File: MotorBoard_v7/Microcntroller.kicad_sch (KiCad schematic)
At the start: 30 parts, among them J1 5Vsel, J10 XDS_VCC, J2 1725656, J2_J4 LaunchPad, J3_J1 LaunchPad, J5 KK-396, J6 11.1V, U1 LM2596S-5.0_NOPB, U2 LM2937ESX-3.3_NOPB, U3 SSD1306

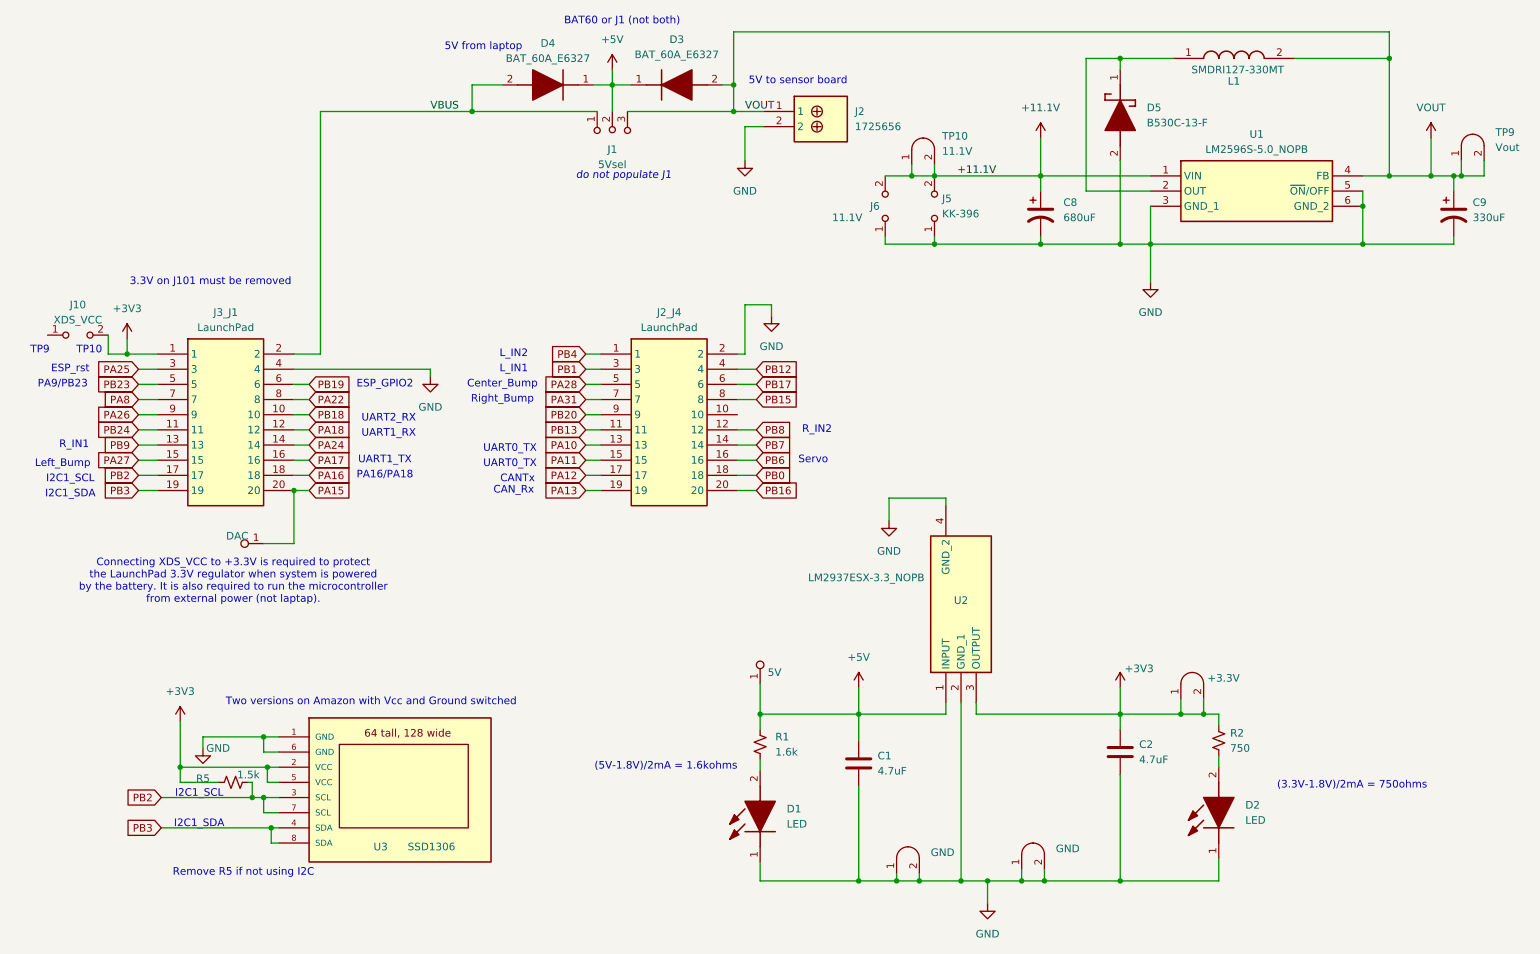
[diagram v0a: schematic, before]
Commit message: added lab 6 update starter files
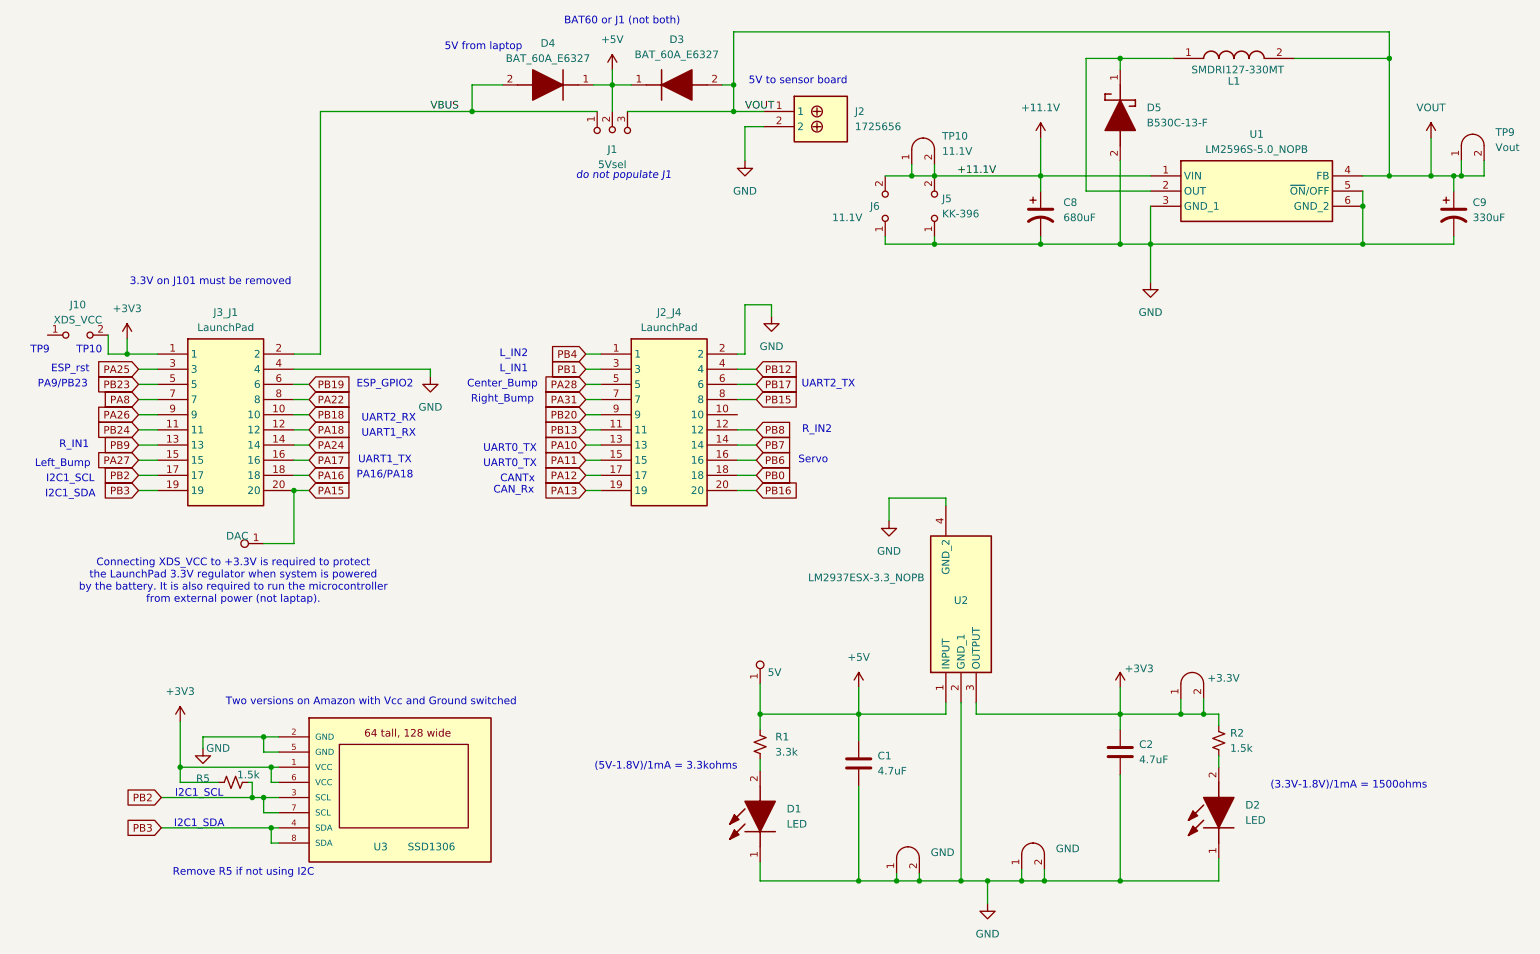
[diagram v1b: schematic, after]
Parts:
- R1: value 1.6k -> 3.3k
- R2: value 750 -> 1.5k
- U3: footprint RSLK2:SSD1306 -> ECE445L:SSD1306; symbol RSLK2:SSD1306 -> ECE445L:SSD1306
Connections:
- net +3V3: now also U3.1 (VCC), U3.6 (VCC); no longer U3.2 (VCC), U3.5 (VCC)
- net GND: now also U3.2 (GND), U3.5 (GND); no longer U3.1 (GND), U3.6 (GND)
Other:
- note added: "(3.3V-1.8V)/1mA = 1500ohms"
- note added: "(5V-1.8V)/1mA = 3.3kohms"
- note added: "UART2_TX"
- note removed: "(3.3V-1.8V)/2mA = 750ohms"
- note removed: "(5V-1.8V)/2mA = 1.6kohms"
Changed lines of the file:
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@@
 	(title_block
 		(title "ECE445M Motor Board")
-		(date "2025-12-23")
-		(rev "v7")
+		(date "2026-01-24")
+		(rev "v7.1")
 		(company "The University of Texas at Austin")
 		(comment 1 "Jonathan Valvano")
@@
 		)
 	)
-	(text "(5V-1.8V)/2mA = 1.6kohms"
+	(text "(5V-1.8V)/1mA = 3.3kohms"
 		(exclude_from_sim no)
 		(at 130.81 140.335 0)
@@
 		)
 	)
-	(text "(3.3V-1.8V)/2mA = 750ohms"
+	(text "(3.3V-1.8V)/1mA = 1500ohms"
 		(exclude_from_sim no)
 		(at 246.38 143.51 0)
@@
 		)
 	)
+	(text "UART2_TX"
+		(exclude_from_sim no)
+		(at 146.05 75.565 0)
+		(effects
+			(font
+				(size 1.27 1.27)
+			)
+		)
+	)
 	(text "UART0_TX"
 		(exclude_from_sim no)
@@
 	)
 	(junction
-		(at 52.07 139.7)
+		(at 250.825 40.64)
 		(diameter 0)
 		(color 0 0 0 0)
 	)
 	(junction
-		(at 250.825 40.64)
+		(at 37.465 139.7)
 		(diameter 0)
 		(color 0 0 0 0)
 	)
 	(junction
-		(at 37.465 139.7)
+		(at 51.435 134.62)
 		(diameter 0)
 		(color 0 0 0 0)
@@
 	)
 	(junction
+		(at 52.705 139.7)
+		(diameter 0)
+		(color 0 0 0 0)
+	)
+	(junction
 		(at 52.705 149.86)
 		(diameter 0)
@@
 	)
 	(junction
-		(at 51.435 134.62)
-		(diameter 0)
-		(color 0 0 0 0)
-	)
-	(junction
 		(at 200.025 52.07)
 		(diameter 0)
@@
 	(wire
 		(pts
+			(xy 53.975 137.16) (xy 51.435 137.16)
+		)
+		(stroke
+			(width 0)
+			(type default)
+		)
+	)
+	(wire
+		(pts
 			(xy 130.175 29.845) (xy 135.255 29.845)
 		)
@@
 	(wire
 		(pts
+			(xy 51.435 134.62) (xy 53.975 134.62)
+		)
+		(stroke
+			(width 0)
+			(type default)
+		)
+	)
+	(wire
+		(pts
+			(xy 41.275 134.62) (xy 51.435 134.62)
+		)
+		(stroke
+			(width 0)
+			(type default)
+		)
+	)
+	(wire
+		(pts
 			(xy 105.41 75.565) (xy 107.95 75.565)
 		)
@@
 	(wire
 		(pts
-			(xy 52.07 139.7) (xy 53.975 139.7)
-		)
-		(stroke
-			(width 0)
-			(type default)
-		)
-	)
-	(wire
-		(pts
-			(xy 53.975 137.16) (xy 51.435 137.16)
-		)
-		(stroke
-			(width 0)
-			(type default)
-		)
-	)
-	(wire
-		(pts
 			(xy 240.03 20.955) (xy 240.03 40.64)
 		)
@@
 	(wire
 		(pts
-			(xy 53.975 142.24) (xy 52.07 142.24)
-		)
-		(stroke
-			(width 0)
-			(type default)
-		)
-	)
-	(wire
-		(pts
 			(xy 194.945 20.955) (xy 203.835 20.955)
 		)
@@
 	(wire
 		(pts
-			(xy 37.465 139.7) (xy 52.07 139.7)
+			(xy 37.465 139.7) (xy 52.705 139.7)
 		)
 		(stroke
@@
 	(wire
 		(pts
-			(xy 51.435 134.62) (xy 53.975 134.62)
+			(xy 255.905 40.64) (xy 252.095 40.64)
 		)
 		(stroke
@@
 	(wire
 		(pts
-			(xy 255.905 40.64) (xy 252.095 40.64)
+			(xy 105.41 73.025) (xy 107.95 73.025)
 		)
 		(stroke
@@
 	(wire
 		(pts
-			(xy 105.41 73.025) (xy 107.95 73.025)
+			(xy 157.48 157.48) (xy 157.48 158.75)
 		)
 		(stroke
@@
 	(wire
 		(pts
-			(xy 157.48 157.48) (xy 157.48 158.75)
+			(xy 194.945 20.955) (xy 194.945 22.86)
 		)
 		(stroke
@@
 	(wire
 		(pts
-			(xy 194.945 20.955) (xy 194.945 22.86)
+			(xy 53.975 142.24) (xy 52.705 142.24)
 		)
 		(stroke
@@
 	(wire
 		(pts
+			(xy 52.705 139.7) (xy 53.975 139.7)
+		)
+		(stroke
+			(width 0)
+			(type default)
+		)
+	)
+	(wire
+		(pts
 			(xy 136.525 62.23) (xy 136.525 64.135)
 		)
@@
 	(wire
 		(pts
-			(xy 52.07 142.24) (xy 52.07 139.7)
+			(xy 130.81 73.025) (xy 133.985 73.025)
 		)
 		(stroke
@@
 	(wire
 		(pts
-			(xy 51.435 137.16) (xy 51.435 134.62)
+			(xy 56.515 73.025) (xy 79.375 73.025)
 		)
 		(stroke
@@
 	(wire
 		(pts
-			(xy 130.81 73.025) (xy 133.985 73.025)
+			(xy 130.81 75.565) (xy 133.985 75.565)
 		)
 		(stroke
@@
 	(wire
 		(pts
-			(xy 56.515 73.025) (xy 79.375 73.025)
+			(xy 51.435 137.16) (xy 51.435 134.62)
 		)
 		(stroke
@@
 	(wire
 		(pts
-			(xy 130.81 75.565) (xy 133.985 75.565)
+			(xy 52.705 142.24) (xy 52.705 139.7)
 		)
 		(stroke
@@
 	(wire
 		(pts
-			(xy 41.275 134.62) (xy 51.435 134.62)
-		)
-		(stroke
-			(width 0)
-			(type default)
-		)
-	)
-	(wire
-		(pts
 			(xy 194.945 52.07) (xy 181.61 52.07)
 		)
@@
 			)
 		)
-		(property "Value" "1.6k"
+		(property "Value" "3.3k"
 			(at 137.16 137.1599 0)
 			(effects
@@
 	)
 	(symbol
-		(lib_id "RSLK2:SSD1306")
+		(lib_id "ECE445L:SSD1306")
 		(at 74.295 146.685 0)
 		(unit 1)
@@
 			)
 		)
-		(property "Footprint" "RSLK2:SSD1306"
+		(property "Footprint" "ECE445L:SSD1306"
 			(at 69.215 123.825 0)
 			(effects
@@
 			)
 		)
-		(property "Value" "750"
+		(property "Value" "1.5k"
 			(at 213.36 136.5249 0)
 			(effects
